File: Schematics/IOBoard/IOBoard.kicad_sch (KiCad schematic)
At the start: 10 parts, among them J1 OLED, J2 Prog, J3 Main_output, J4 MainBoard, J5 SW(C/D), U1 ATSAMD09D14A-M

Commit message: IOBoard completed
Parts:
- removed J5: SW(C/D), Connector_PinHeader_2.54mm:PinHeader_1x02_P2.54mm_Vertical, symbol Connector:Conn_01x02_Female
- removed R1: 10k, Resistor_SMD:R_0603_1608Metric, symbol Device:R_Small
- removed U1: ATSAMD09D14A-M, Package_DFN_QFN:QFN-24-1EP_4x4mm_P0.5mm_EP2.6x2.6mm, symbol MCU_Microchip_SAMD:ATSAMD09D14A-M
- added JP1: D0, Jumper:SolderJumper-3_P1.3mm_Bridged12_Pad1.0x1.5mm, symbol Jumper:Jumper_3_Bridged12
- added JP2, JP3: D1, Jumper:SolderJumper-3_P1.3mm_Bridged12_Pad1.0x1.5mm, symbol Jumper:Jumper_3_Bridged12
- added R2: 10k, Resistor_SMD:R_0603_1608Metric, symbol Device:R_Small
- added U1: ATSAMD21E18A-M, Package_DFN_QFN:QFN-32-1EP_5x5mm_P0.5mm_EP3.6x3.6mm, symbol MCU_Microchip_SAMD:ATSAMD21E18A-M
- C1: value 0.1uF -> 1uF
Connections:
- net I2C_SDA_IN is gone; now on net SEL2: J4.5 (Pin_5)
- net +3V3: now also J2.5 (Pin_5), J4.6 (Pin_6), R2.1, U1.30 (VDDIN), U1.9 (VDDANA); no longer C1.2, J2.1 (Pin_1), J4.1 (Pin_1)
- net GND: now also C1.2, J2.3 (Pin_3), J4.10 (Pin_10), U1.10 (GND), U1.28 (GND); no longer C1.1, J2.5 (Pin_5), J2.6 (Pin_6), J4.2 (Pin_2), J4.3 (Pin_3), J4.9 (Pin_9)
- net RESET: now also J4.8 (Pin_8), R2.2, U1.26 (~RESET); no longer J2.2 (Pin_2), J4.4 (Pin_4)
- net SEL1: now also J4.9 (Pin_9), U1.19 (PA18); no longer J4.6 (Pin_6)
- net SEL2: now also U1.20 (PA19); no longer J4.10 (Pin_10), J4.8 (Pin_8)
- net SWC: now also J2.2 (Pin_2), U1.31 (PA30); no longer J2.3 (Pin_3)
- net SWD: now also J2.1 (Pin_1), U1.32 (PA31); no longer J2.4 (Pin_4)
- net at D1.1 (DI): now also U1.14 (PA11)
- net at D1.2 (CI): now also U1.13 (PA10)
- net DAC/ADC/1-Wire renamed OUTPUT
- net OUTPUT: now also JP3.2 (C)
- net I2C_SCL_IN renamed SEL0
- net SEL0: now also U1.18 (PA17)
- net I2C_SCL_OUT renamed OLED_SCL_I2C
- net OLED_SCL_I2C: now also U1.2 (PA01)
- net I2C_SDA_OUT renamed OLED_SDA_I2C
- net OLED_SDA_I2C: now also U1.1 (PA00)
- new net: C1.1, U1.29 (VDDCORE)
- new net D0: J4.1 (Pin_1), JP1.2 (C)
- new net D0_I2C: JP1.1 (A), U1.12 (PA09)
- new net D0_SPI: JP1.3 (B), U1.5 (PA04)
- new net D1: J4.2 (Pin_2), JP2.2 (C)
- new net D1_I2C: JP2.1 (A), U1.11 (PA08)
- new net D1_SPI: JP2.3 (B), U1.8 (PA07)
- new net DAC/ADC: JP3.3 (B), U1.3 (PA02)
- new net RX: J2.4 (Pin_4), U1.22 (PA23)
- new net SCK: J4.4 (Pin_4), U1.6 (PA05)
- new net SS: J4.3 (Pin_3), U1.7 (PA06)
- new net TX: J2.6 (Pin_6), U1.21 (PA22)
- new net TX/RX: JP3.1 (A), U1.17 (PA16)
- no-connect marks 2 -> 9
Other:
- note added: "I2C/SPI jumpers"
- note added: "MISO"
- note added: "MOSI"
- note added: "Main output"
- note added: "Microcontroller"
- note added: "SCL"
- note added: "SDA"
- note removed: "MCU"
- note removed: "Output terminal"
- moved on the sheet: D1, J1, J2, J3

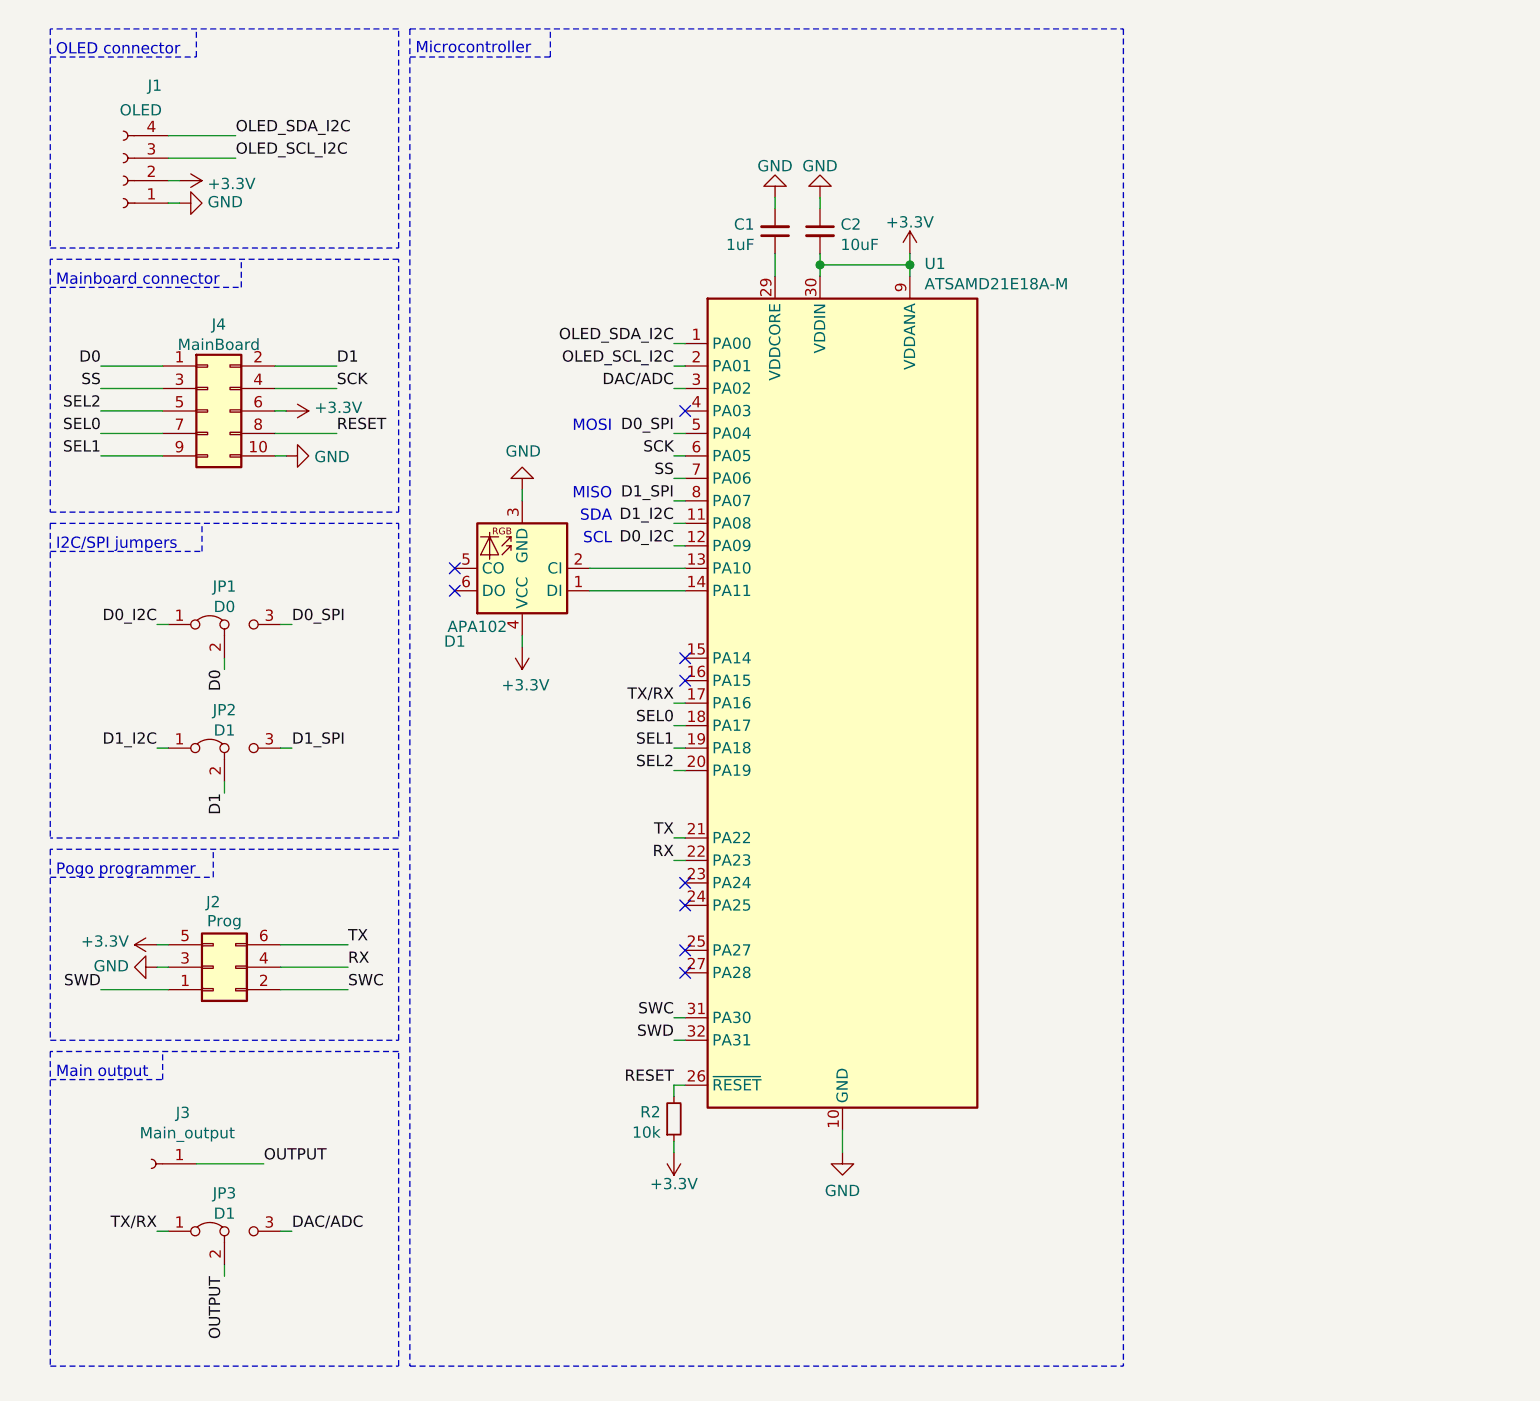
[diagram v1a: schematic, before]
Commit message: Finished circuit - pre mousebites
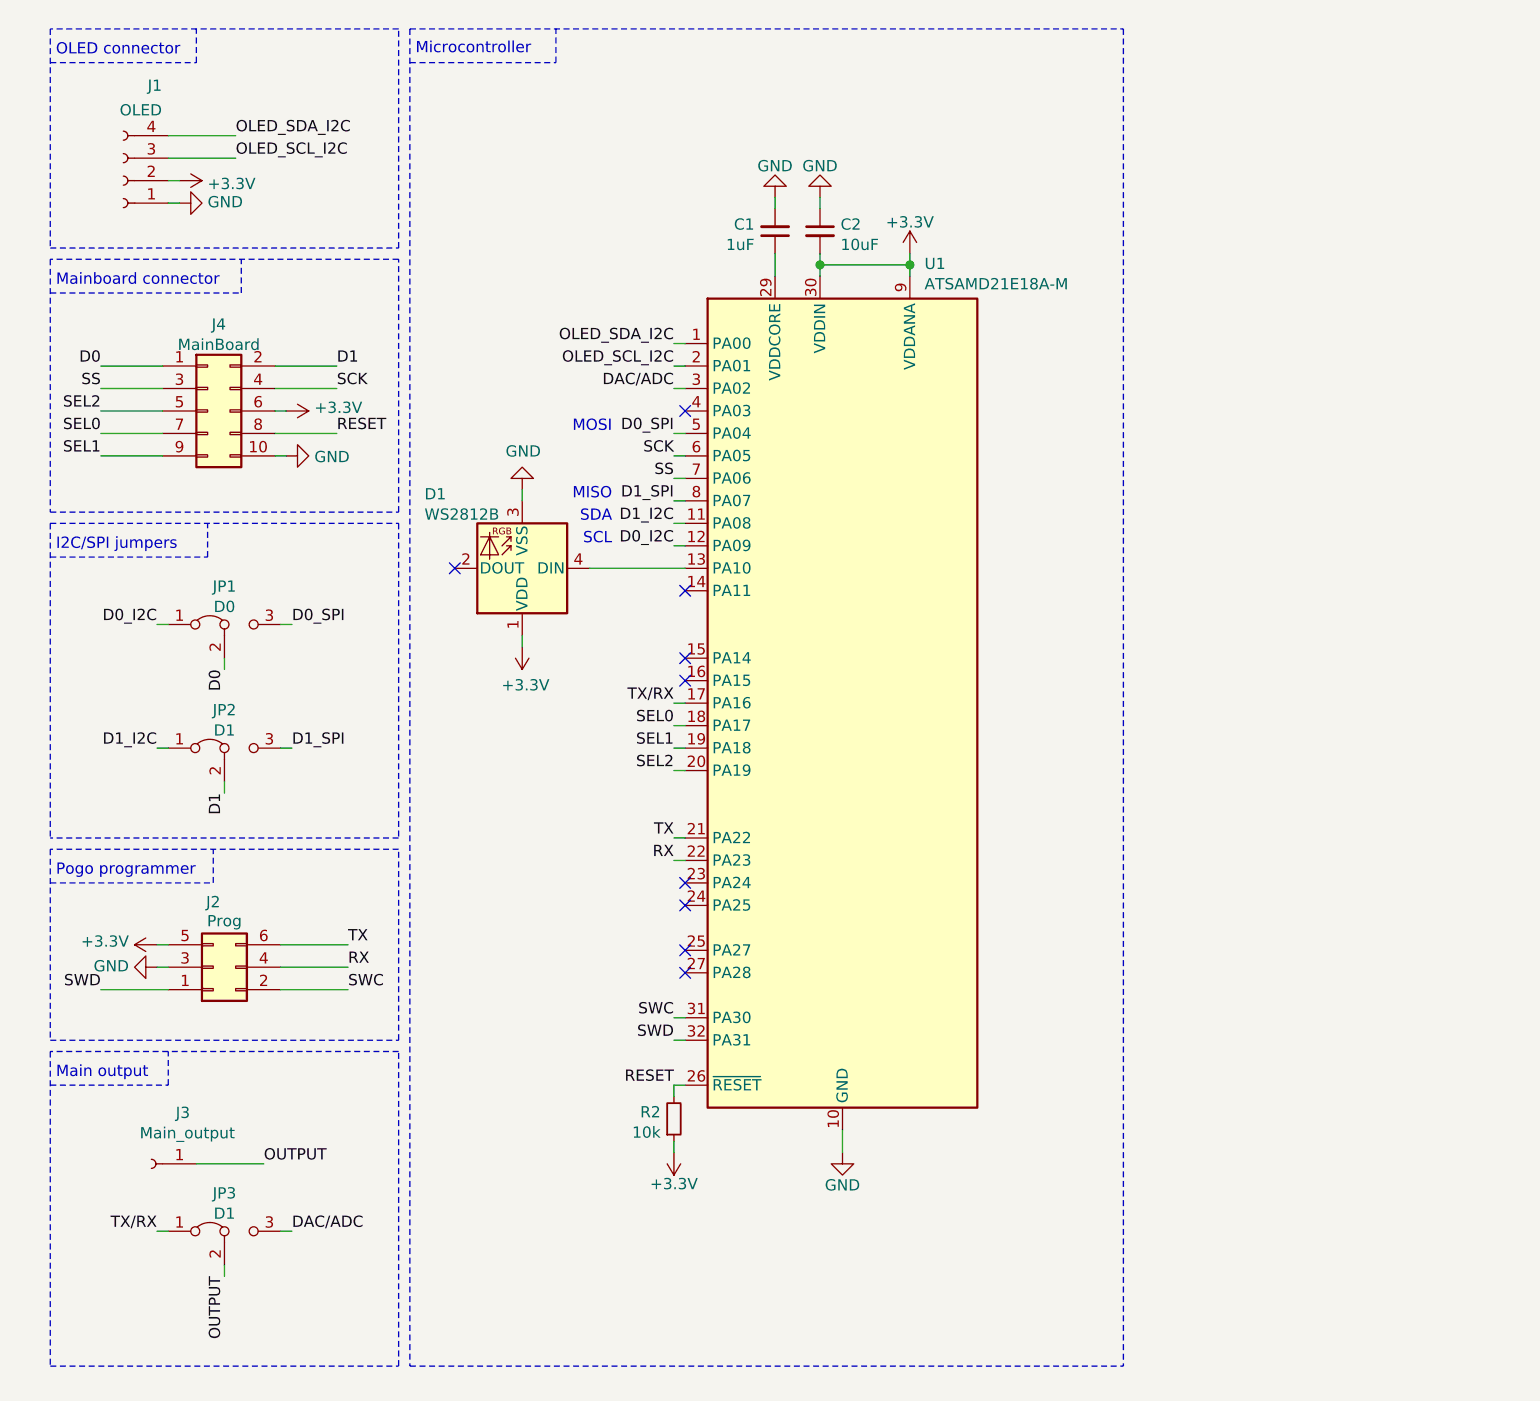
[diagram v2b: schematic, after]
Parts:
- removed D1: APA102, LED_SMD:LED_RGB_5050-6, symbol LED:APA102
- added D1: WS2812B, LED_SMD:LED_WS2812B_PLCC4_5.0x5.0mm_P3.2mm, symbol LED:WS2812B
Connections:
- net +3V3: now also D1.1 (VDD)
- net GND: now also D1.3 (VSS)
- net at U1.13 (PA10): now also D1.4 (DIN)
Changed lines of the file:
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@@
   (junction (at 110.49 40.005) (diameter 1.016) (color 0 0 0 0))
   (no_connect (at 59.055 74.295))
-  (no_connect (at 59.055 76.835))
   (no_connect (at 85.09 56.515))
+  (no_connect (at 85.09 76.835))
   (no_connect (at 85.09 84.455))
   (no_connect (at 85.09 86.995))
@@
     (stroke (width 0) (type solid) (color 0 0 0 0))
   )
-  (wire (pts (xy 74.295 76.835) (xy 85.09 76.835))
-    (stroke (width 0) (type solid) (color 0 0 0 0))
-  )
   (wire (pts (xy 83.82 48.895) (xy 85.09 48.895))
     (stroke (width 0) (type solid) (color 0 0 0 0))
@@
     (stroke (width 0) (type dash) (color 0 0 0 0))
   )
-  (polyline (pts (xy 13.335 16.51) (xy 29.845 16.51))
+  (polyline (pts (xy 13.335 17.145) (xy 29.845 17.145))
     (stroke (width 0) (type dash) (color 0 0 0 0))
   )
@@
     (stroke (width 0) (type dash) (color 0 0 0 0))
   )
-  (polyline (pts (xy 13.335 42.545) (xy 34.925 42.545))
+  (polyline (pts (xy 13.335 43.18) (xy 34.925 43.18))
     (stroke (width 0) (type dash) (color 0 0 0 0))
   )
@@
     (stroke (width 0) (type dash) (color 0 0 0 0))
   )
-  (polyline (pts (xy 13.335 72.39) (xy 30.48 72.39))
+  (polyline (pts (xy 13.335 73.025) (xy 31.115 73.025))
     (stroke (width 0) (type dash) (color 0 0 0 0))
   )
@@
     (stroke (width 0) (type dash) (color 0 0 0 0))
   )
-  (polyline (pts (xy 13.335 109.22) (xy 31.75 109.22))
+  (polyline (pts (xy 13.335 109.855) (xy 31.75 109.855))
     (stroke (width 0) (type dash) (color 0 0 0 0))
   )
@@
     (stroke (width 0) (type dash) (color 0 0 0 0))
   )
-  (polyline (pts (xy 13.335 132.08) (xy 26.035 132.08))
+  (polyline (pts (xy 13.335 132.715) (xy 26.67 132.715))
     (stroke (width 0) (type dash) (color 0 0 0 0))
   )
@@
     (stroke (width 0) (type dash) (color 0 0 0 0))
   )
-  (polyline (pts (xy 26.035 132.08) (xy 26.035 128.905))
-    (stroke (width 0) (type dash) (color 0 0 0 0))
-  )
-  (polyline (pts (xy 29.845 16.51) (xy 29.845 13.335))
-    (stroke (width 0) (type dash) (color 0 0 0 0))
-  )
-  (polyline (pts (xy 30.48 72.39) (xy 30.48 69.215))
-    (stroke (width 0) (type dash) (color 0 0 0 0))
-  )
-  (polyline (pts (xy 31.75 109.22) (xy 31.75 106.045))
-    (stroke (width 0) (type dash) (color 0 0 0 0))
-  )
-  (polyline (pts (xy 34.925 42.545) (xy 34.925 39.37))
+  (polyline (pts (xy 26.67 132.715) (xy 26.67 128.905))
+    (stroke (width 0) (type dash) (color 0 0 0 0))
+  )
+  (polyline (pts (xy 29.845 17.145) (xy 29.845 13.335))
+    (stroke (width 0) (type dash) (color 0 0 0 0))
+  )
+  (polyline (pts (xy 31.115 73.025) (xy 31.115 69.215))
+    (stroke (width 0) (type dash) (color 0 0 0 0))
+  )
+  (polyline (pts (xy 31.75 109.855) (xy 31.75 106.045))
+    (stroke (width 0) (type dash) (color 0 0 0 0))
+  )
+  (polyline (pts (xy 34.925 43.18) (xy 34.925 39.37))
     (stroke (width 0) (type dash) (color 0 0 0 0))
   )
@@
     (stroke (width 0) (type dash) (color 0 0 0 0))
   )
-  (polyline (pts (xy 53.975 16.51) (xy 69.85 16.51))
+  (polyline (pts (xy 53.975 17.145) (xy 70.485 17.145))
     (stroke (width 0) (type dash) (color 0 0 0 0))
   )
@@
     (stroke (width 0) (type dash) (color 0 0 0 0))
   )
-  (polyline (pts (xy 69.85 16.51) (xy 69.85 13.335))
+  (polyline (pts (xy 70.485 17.145) (xy 70.485 13.335))
     (stroke (width 0) (type dash) (color 0 0 0 0))
   )
@@
       (effects (font (size 1.27 1.27)) hide)
     )
-    (property "Value" "GND" (id 1) (at 102.87 144.6594 0))
+    (property "Value" "GND" (id 1) (at 102.87 144.0244 0))
     (property "Footprint" "" (id 2) (at 102.87 140.335 0)
       (effects (font (size 1.27 1.27)) hide)
@@
     (pin "9")
   )
-  (symbol (lib_id "LED:APA102") (at 66.675 74.295 180) (unit 1)
-    (in_bom yes) (on_board yes)
-    (property "Reference" "D1" (id 0) (at 59.055 82.5692 0))
-    (property "Value" "APA102" (id 1) (at 61.595 80.9055 0))
-    (property "Footprint" "LED_SMD:LED_RGB_5050-6" (id 2) (at 65.405 66.675 0)
+  (symbol (lib_id "LED:WS2812B") (at 66.675 74.295 180) (unit 1)
+    (in_bom yes) (on_board yes)
+    (property "Reference" "D1" (id 0) (at 55.6261 65.9141 0)
+      (effects (font (size 1.27 1.27)) (justify right))
+    )
+    (property "Value" "WS2812B" (id 1) (at 55.6261 68.2128 0)
+      (effects (font (size 1.27 1.27)) (justify right))
+    )
+    (property "Footprint" "LED_SMD:LED_WS2812B_PLCC4_5.0x5.0mm_P3.2mm" (id 2) (at 65.405 66.675 0)
       (effects (font (size 1.27 1.27)) (justify left top) hide)
     )
-    (property "Datasheet" "http://www.led-color.com/upload/201506/APA102%20LED.pdf" (id 3) (at 64.135 64.77 0)
+    (property "Datasheet" "https://cdn-shop.adafruit.com/datasheets/WS2812B.pdf" (id 3) (at 64.135 64.77 0)
       (effects (font (size 1.27 1.27)) (justify left top) hide)
     )
@@
     (pin "3")
     (pin "4")
-    (pin "5")
-    (pin "6")
   )
   (symbol (lib_id "MCU_Microchip_SAMD:ATSAMD21E18A-M") (at 102.87 89.535 0) (unit 1)
@@
       (reference "C2") (unit 1) (value "10uF") (footprint "Capacitor_SMD:C_0603_1608Metric")
     )
-    (path "/5b36ff10-ccba-4630-a829-a1ae9fecaa30"
-      (reference "D1") (unit 1) (value "APA102") (footprint "LED_SMD:LED_RGB_5050-6")
+    (path "/7d11955e-2096-43bf-ae13-ee7d22f498f7"
+      (reference "D1") (unit 1) (value "WS2812B") (footprint "LED_SMD:LED_WS2812B_PLCC4_5.0x5.0mm_P3.2mm")
     )
     (path "/f499ddb7-2f15-4704-bac4-3a64cc020b4e"
